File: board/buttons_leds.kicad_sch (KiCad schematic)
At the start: 12 parts, among them SW401 POWER, SW402 VOL+, SW403 VOL-

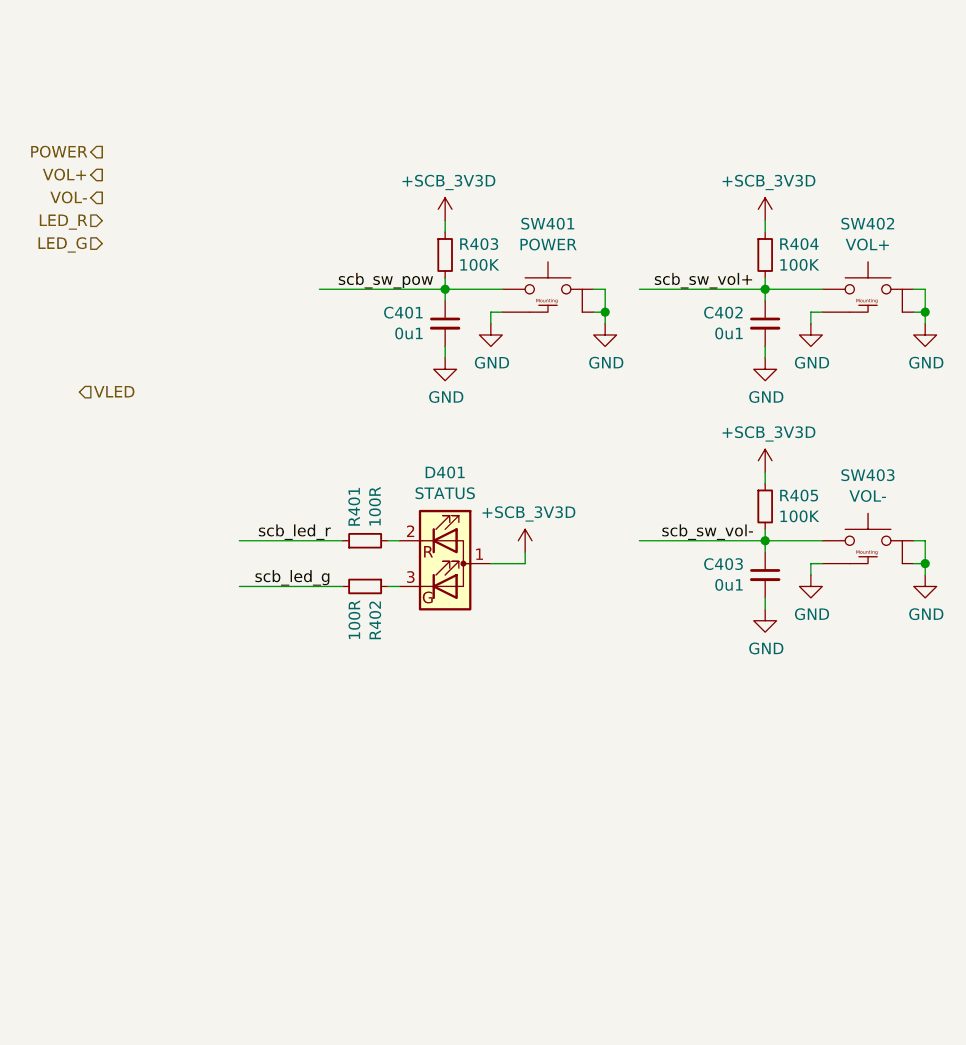
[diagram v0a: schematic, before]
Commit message: Added testpoints and other fixes
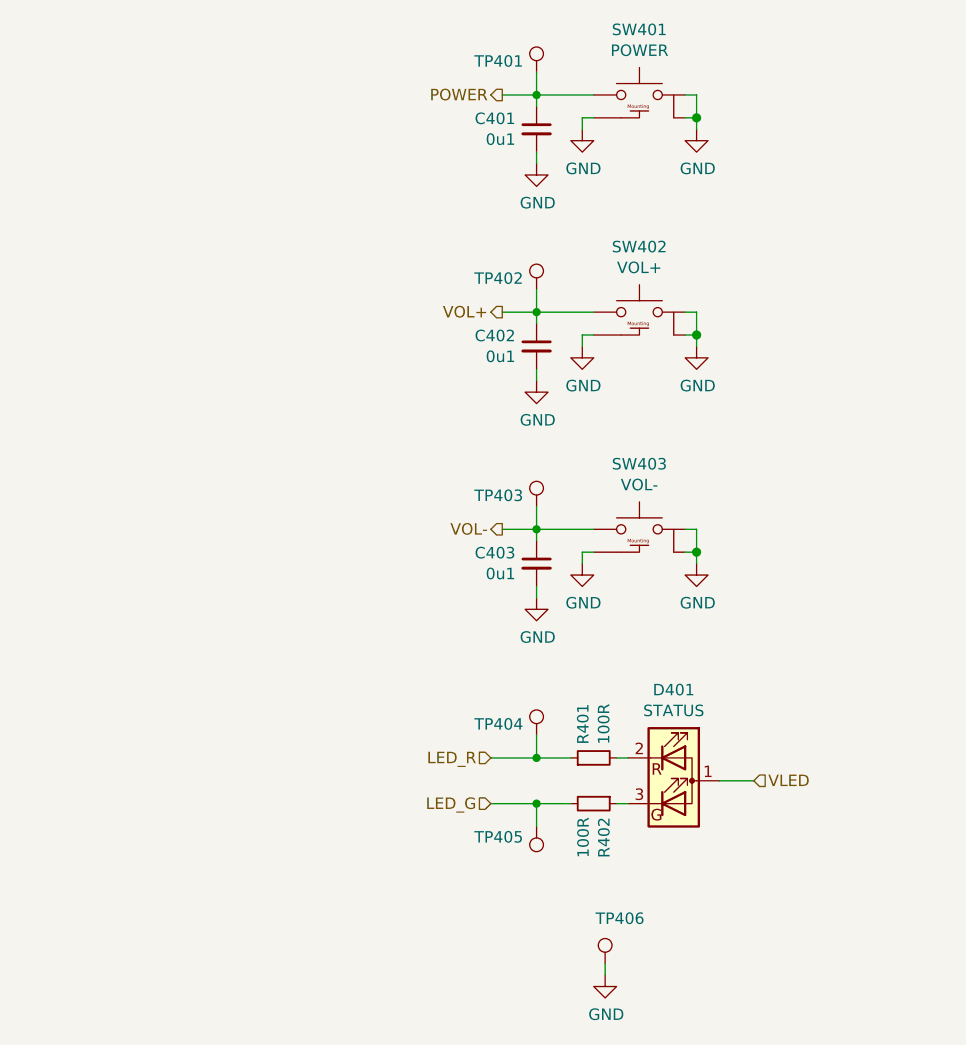
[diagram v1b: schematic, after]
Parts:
- removed R403, R404, R405: 100K, DIYPie:R_0402_1005Metric, symbol Device:R_Small
- added TP401, TP402, TP403, TP404, TP405, TP406: TestPoint, DIYPie:TestPoint_Pad_D1.5mm, symbol DIYPie:TestPoint
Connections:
- net +3V3 is gone; now on net VLED: D401.1 (A)
- net scb_led_g is gone; now on net LED_G: R402.2
- net scb_led_r is gone; now on net LED_R: R401.1
- net scb_sw_pow is gone; now on net POWER: C401.1, SW401.2
- net scb_sw_vol+ is gone; now on net VOL+: C402.1, SW402.2
- net scb_sw_vol- is gone; now on net VOL-: C403.1, SW403.2
- net GND: now also TP406.1
- net LED_G: now also TP405.1
- net LED_R: now also TP404.1
- net POWER: now also TP401.1
- net VOL+: now also TP402.1
- net VOL-: now also TP403.1
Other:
- moved on the sheet: C401, C402, C403, D401, R401, R402, SW401, SW402, SW403
